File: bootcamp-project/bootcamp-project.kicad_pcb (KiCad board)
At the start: 2 copper layers, 17 parts, among them J3 FTDI, SW1 SW_Push, U1 ATmega328P-A, Y1 16MHz

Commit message: pcb: not viable
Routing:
- net TXO: track 0.00 -> 64.6 mm, vias 0 -> 2
- net MOSI: track 0.00 -> 60.5 mm, vias 0 -> 2
- net D7: track 0.00 -> 54.2 mm
- net D8: track 0.00 -> 53.9 mm, vias 0 -> 1
- net RXI: track 0.00 -> 50.1 mm, vias 0 -> 1
- net RAW: track 0.00 -> 37.7 mm, vias 0 -> 2
- net MISO: track 0.00 -> 31.2 mm, vias 0 -> 1
- net D6: track 0.00 -> 29.9 mm, vias 0 -> 1
- net D5: track 0.00 -> 24.0 mm, vias 0 -> 1
- net D4: track 0.00 -> 16.0 mm, vias 0 -> 1
- net D2: track 0.00 -> 15.4 mm, vias 0 -> 1
- net D3: track 0.00 -> 13.1 mm, vias 0 -> 1
- net GND: track 89.0 -> 92.7 mm, vias 3 -> 2
- net SCK: track 48.2 -> 44.7 mm, vias 1 -> 2
- net DTR: track 57.1 -> 58.5 mm

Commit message: pcb: new try, again
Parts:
- moved R2 24.8 mm to (99.6, 97.5), turned to 135 degrees
- moved C2 22.7 mm to (120.3, 78.7)
- moved D2 20.8 mm to (101.0, 96.1), turned to 135 degrees
- moved C3 18.7 mm to (119.8, 91.2), turned to 0 degrees
- moved R3 15.1 mm to (100.8, 79.1), turned to 0 degrees
- moved R1 10.5 mm to (115.8, 78.8), turned to 0 degrees
- moved D1 9.36 mm to (115.8, 76.4), turned to 0 degrees
- moved SW1 9.28 mm to (119.5, 101.0)
- moved C1 8.31 mm to (119.9, 83.9)
- moved C4 8.06 mm to (112.1, 101.1)
- moved C6 6.10 mm to (106.7, 101.1), turned to 0 degrees
- moved J1 4.00 mm to (95.0, 91.2)
- moved U1 3.61 mm to (109.4, 88.8), turned to -135 degrees
- moved J2 3.00 mm to (125.0, 92.5)
- moved C7 2.01 mm to (102.9, 94.2)
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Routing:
- net MOSI: track 60.5 -> 0.00 mm, vias 2 -> 0
- net D7: track 54.2 -> 0.00 mm
- net D8: track 53.9 -> 0.00 mm, vias 1 -> 0
- net DTR: track 58.5 -> 12.3 mm, vias 2 -> 0
- net SCK: track 44.7 -> 0.00 mm, vias 2 -> 0
- net TXO: track 64.6 -> 23.1 mm, vias 2 -> 0
- net RAW: track 37.7 -> 70.7 mm, vias 2 -> 0
- net MISO: track 31.2 -> 0.00 mm, vias 1 -> 0
- net D6: track 29.9 -> 0.00 mm, vias 1 -> 0
- net D5: track 24.0 -> 0.00 mm, vias 1 -> 0
- net RXI: track 50.1 -> 29.3 mm, vias 1 -> 0
- net D4: track 16.0 -> 0.00 mm, vias 1 -> 0
- net D2: track 15.4 -> 0.00 mm, vias 1 -> 0
- net D3: track 13.1 -> 0.00 mm, vias 1 -> 0
- net Net-(U1-XTAL2/PB7): track 13.0 -> 0.00 mm
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
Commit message: pcb: everything seems connected
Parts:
- moved C2 1.25 mm to (120.3, 80.0)
- moved D1 1.25 mm to (115.8, 77.7)
- moved R1 1.25 mm to (115.8, 80.0)
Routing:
- net DTR: track 12.3 -> 81.1 mm, vias 0 -> 4
- net TXO: track 23.1 -> 76.0 mm, vias 0 -> 1
- net RXI: track 29.3 -> 75.6 mm
- net SCK: track 0.00 -> 39.5 mm, vias 0 -> 3
- net D2: track 0.00 -> 30.7 mm
- net D10: track 0.00 -> 26.5 mm, vias 0 -> 1
- net MOSI: track 0.00 -> 25.6 mm, vias 0 -> 1
- net VCC: track 38.9 -> 62.7 mm, vias 0 -> 2
- net Net-(U1-XTAL2/PB7): track 0.00 -> 22.3 mm, vias 0 -> 2
- net Net-(C1-Pad1): track 0.00 -> 20.6 mm, vias 0 -> 2
- net MISO: track 0.00 -> 20.4 mm, vias 0 -> 1
- net D4: track 0.00 -> 19.0 mm, vias 0 -> 1
- net D3: track 0.00 -> 18.7 mm, vias 0 -> 1
- net A3: track 0.00 -> 18.0 mm, vias 0 -> 1
- net D9: track 0.00 -> 17.8 mm, vias 0 -> 1
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
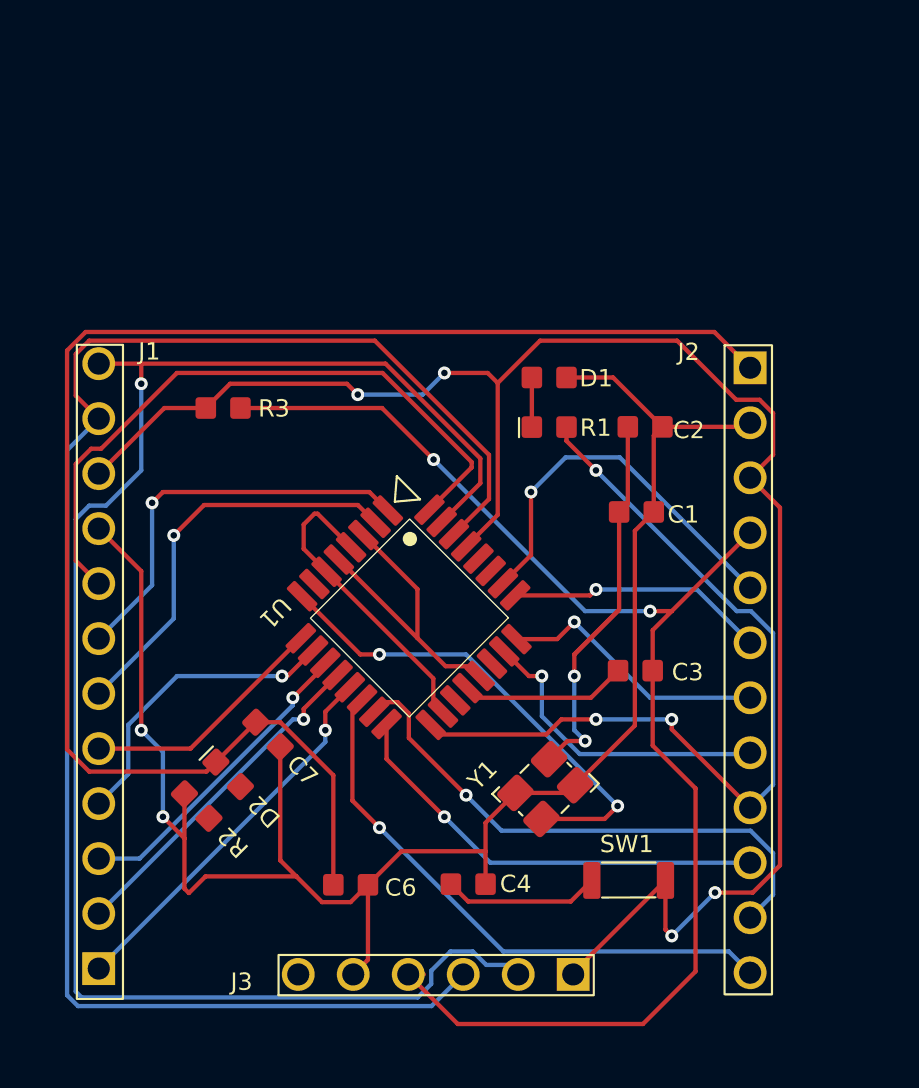
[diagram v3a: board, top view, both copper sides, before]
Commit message: pcb: all connected, no error, no warning
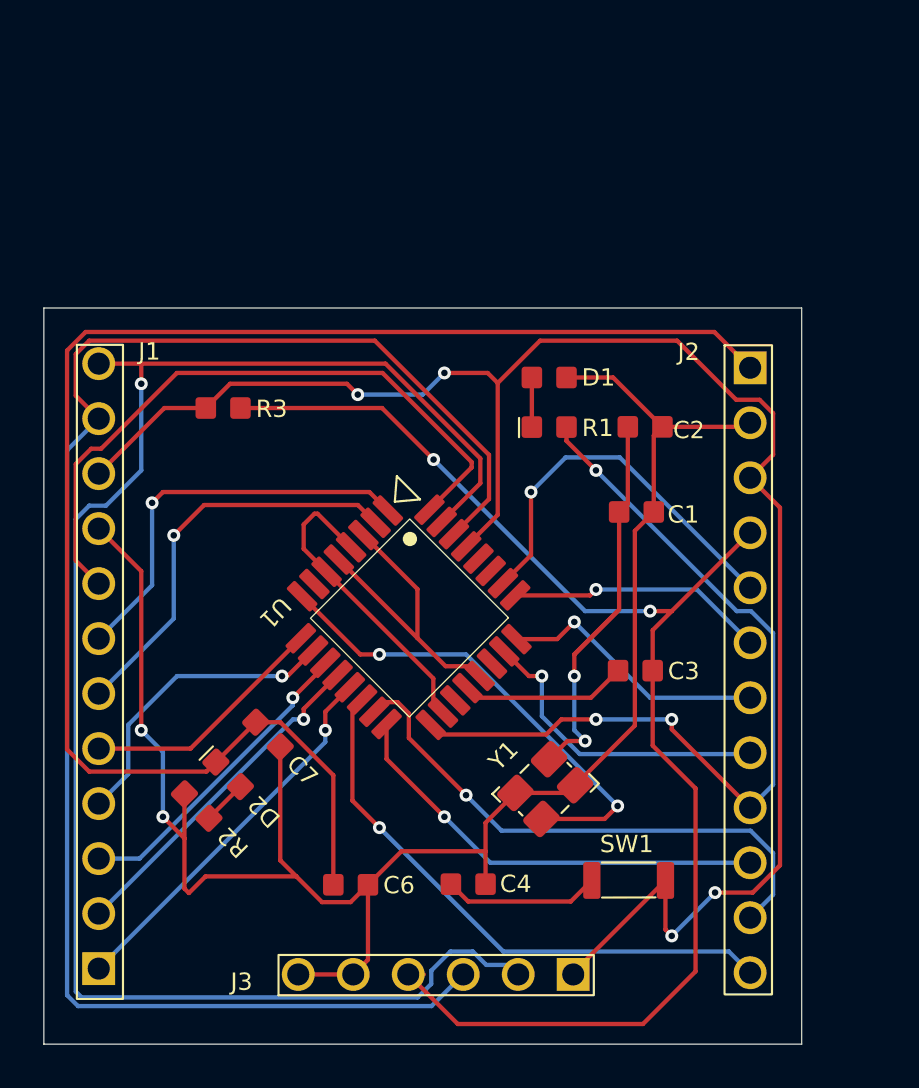
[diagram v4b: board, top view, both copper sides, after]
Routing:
- net GND: track 82.2 -> 84.8 mm
- net Net-(R2-Pad1): track 0.00 -> 2.07 mm
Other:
- board outline added: 35 x 34 mm
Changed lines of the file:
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@@
 		(sheetfile "bootcamp-project.kicad_sch")
 		(attr smd)
-		(fp_poly
-			(pts
-				(xy -1.355 -0.583093) (xy 1.345001 -0.583093) (xy 1.345 0.56) (xy -1.355 0.56)
-			)
+		(fp_rect
+			(start -1.355 -0.583093)
+			(end 1.345 0.56)
 			(stroke
 				(width 0.05)
@@
 		)
 		(fp_text user "R1"
-			(at 1.41 0.49 0)
+			(at 1.5 0.5 0)
 			(unlocked yes)
 			(layer "F.SilkS")
@@
 		)
 		(pad "1" smd roundrect
-			(at -0.81 -0.010001)
+			(at -0.81 -0.01)
 			(size 0.95 1)
 			(layers "F.Cu" "F.Mask" "F.Paste")
@@
 		)
 		(pad "2" smd roundrect
-			(at 0.789999 -0.01)
+			(at 0.79 -0.01)
 			(size 0.95 1)
 			(layers "F.Cu" "F.Mask" "F.Paste")
@@
 		(fp_poly
 			(pts
-				(xy -2 -1.67) (xy -2 1.68) (xy 2.06 1.679999) (xy 2.06 -1.67)
+				(xy -2 -1.67) (xy 2.06 -1.67) (xy 2.06 1.679999) (xy -2 1.68)
 			)
 			(stroke
@@
 		)
 		(fp_text user "Y1"
-			(at -2.265 -2.06 45)
+			(at -0.95 -2.01 45)
 			(unlocked yes)
 			(layer "F.SilkS")
@@
 		(sheetfile "bootcamp-project.kicad_sch")
 		(attr smd)
-		(fp_poly
-			(pts
-				(xy -1.335 -0.579999) (xy 1.355 -0.58) (xy 1.355 0.58) (xy -1.335 0.579999)
-			)
+		(fp_rect
+			(start -1.335 -0.58)
+			(end 1.355 0.58)
 			(stroke
 				(width 0.05)
@@
 		)
 		(fp_text user "C6"
-			(at 1.58 0.61 0)
+			(at 1.5 0.5 0)
 			(unlocked yes)
 			(layer "F.SilkS")
@@
 		)
 		(pad "1" smd roundrect
-			(at -0.799999 0.01)
+			(at -0.8 0.01)
 			(size 0.95 1)
 			(layers "F.Cu" "F.Mask" "F.Paste")
@@
 		)
 		(pad "2" smd roundrect
-			(at 0.799999 0.01)
+			(at 0.8 0.01)
 			(size 0.95 1)
 			(layers "F.Cu" "F.Mask" "F.Paste")
@@
 		(sheetfile "bootcamp-project.kicad_sch")
 		(attr smd)
-		(fp_poly
-			(pts
-				(xy -1.55 -0.56) (xy 1.565 -0.56) (xy 1.565 0.6) (xy -1.55 0.600001)
-			)
+		(fp_rect
+			(start -1.55 -0.56)
+			(end 1.565 0.6)
 			(stroke
 				(width 0.05)
@@
 		)
 		(fp_text user "D1"
-			(at 1.395 0.535 0)
+			(at 1.5 0.5 0)
 			(unlocked yes)
 			(layer "F.SilkS")
@@
 		(sheetfile "bootcamp-project.kicad_sch")
 		(attr smd)
-		(fp_poly
-			(pts
-				(xy -1.335 -0.579999) (xy 1.355 -0.58) (xy 1.355 0.58) (xy -1.335 0.579999)
-			)
+		(fp_rect
+			(start -1.335 -0.58)
+			(end 1.355 0.58)
 			(stroke
 				(width 0.05)
@@
 		)
 		(fp_text user "C3"
-			(at 1.68 0.55 0)
+			(at 1.5 0.5 0)
 			(unlocked yes)
 			(layer "F.SilkS")
@@
 		)
 		(pad "1" smd roundrect
-			(at -0.799999 0.01)
+			(at -0.8 0.01)
 			(size 0.95 1)
 			(layers "F.Cu" "F.Mask" "F.Paste")
@@
 		)
 		(pad "2" smd roundrect
-			(at 0.799999 0.01)
+			(at 0.8 0.01)
 			(size 0.95 1)
 			(layers "F.Cu" "F.Mask" "F.Paste")
@@
 		(sheetfile "bootcamp-project.kicad_sch")
 		(attr smd)
-		(fp_poly
-			(pts
-				(xy -1.355 -0.583093) (xy 1.345001 -0.583093) (xy 1.345 0.56) (xy -1.355 0.56)
-			)
+		(fp_rect
+			(start -1.355 -0.583093)
+			(end 1.345 0.56)
 			(stroke
 				(width 0.05)
@@
 		)
 		(fp_text user "R3"
-			(at 1.61 0.48 0)
+			(at 1.5 0.5 0)
 			(unlocked yes)
 			(layer "F.SilkS")
@@
 		)
 		(pad "1" smd roundrect
-			(at -0.81 -0.010001)
+			(at -0.81 -0.01)
 			(size 0.95 1)
 			(layers "F.Cu" "F.Mask" "F.Paste")
@@
 		)
 		(pad "2" smd roundrect
-			(at 0.789999 -0.01)
+			(at 0.79 -0.01)
 			(size 0.95 1)
 			(layers "F.Cu" "F.Mask" "F.Paste")
@@
 		(layer "F.SilkS")
 	)
+	(gr_rect
+		(start 92.5 74.5)
+		(end 127.5 108.5)
+		(stroke
+			(width 0.05)
+			(type default)
+		)
+		(fill no)
+		(layer "Edge.Cuts")
+	)
 	(segment
 		(start 119.47 79.99)
@@
 	)
 	(segment
+		(start 106.79 105.28)
+		(end 104.25 105.28)
+		(width 0.2)
+		(layer "F.Cu")
+		(net 15)
+	)
+	(segment
 		(start 95.035 84.69)
 		(end 97 86.655)
@@
 	)
 	(segment
+		(start 101.576899 96.604472)
+		(end 100.125685 98.055686)
+		(width 0.2)
+		(layer "F.Cu")
+		(net 27)
+	)
+	(segment
+		(start 100.125685 98.055686)
+		(end 100.125685 98.069828)
+		(width 0.2)
+		(layer "F.Cu")
+		(net 27)
+	)
+	(segment

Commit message: pcb: add ground plane
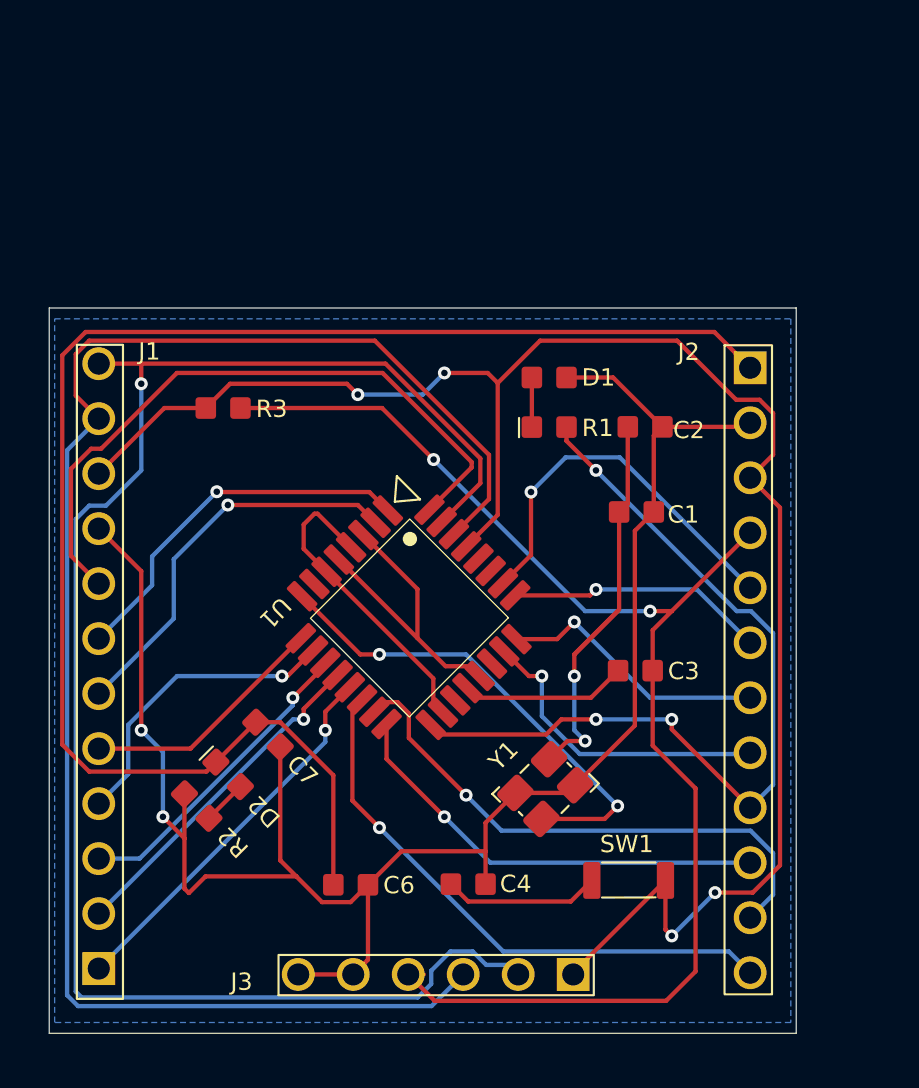
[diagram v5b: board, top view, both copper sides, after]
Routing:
- net D3: track 18.7 -> 17.3 mm
- net VCC: track 62.7 -> 61.8 mm
- net D4: track 19.0 -> 18.3 mm
- added copper zone on B.Cu, net GND
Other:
- board size 35 x 34 mm -> 34.5 x 33.5 mm

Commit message: pcb: remake a clean pcb
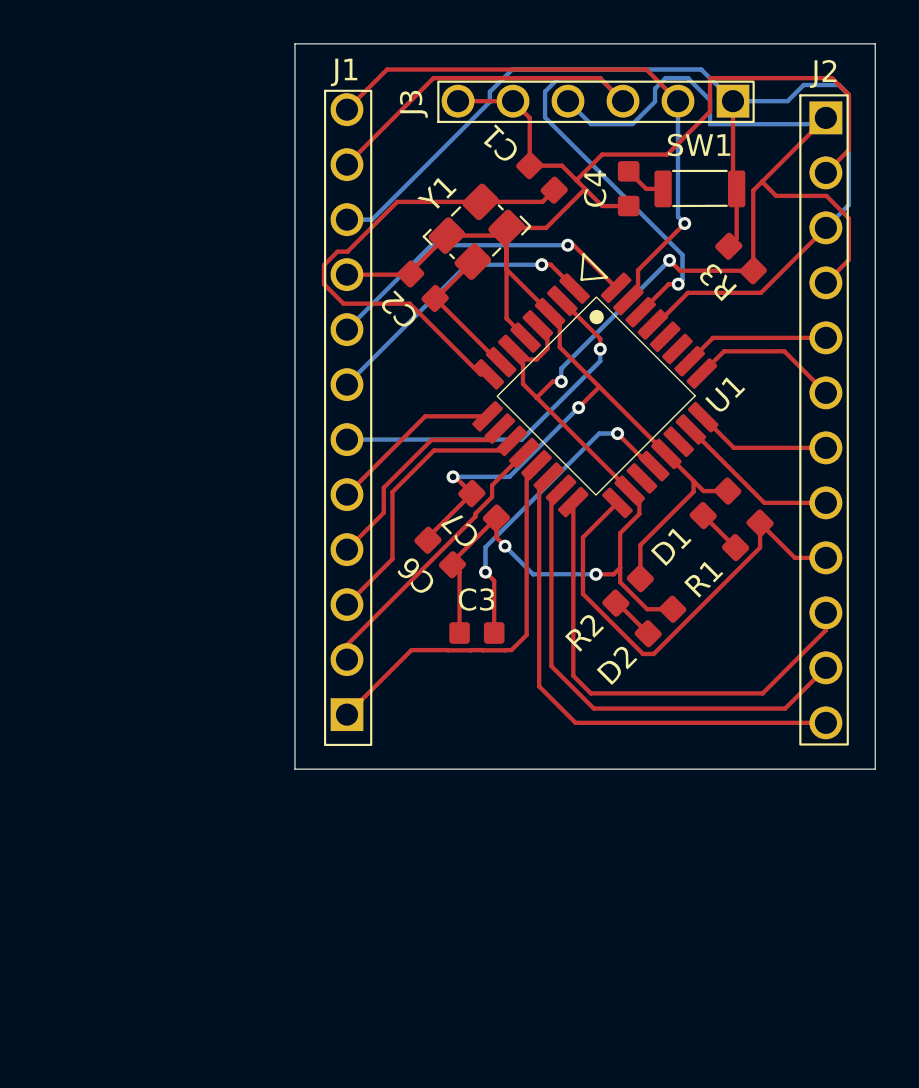
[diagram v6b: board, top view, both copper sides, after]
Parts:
- moved J3 41.0 mm to (118.0, 65.0)
- moved C4 33.0 mm to (119.5, 69.0), turned to 90 degrees
- moved SW1 32.1 mm to (122.8, 69.0)
- moved Y1 25.9 mm to (112.5, 71.0)
- moved R3 24.9 mm to (124.7, 72.2), turned to 135 degrees
- moved R2 22.3 mm to (119.5, 87.6), turned to 45 degrees
- moved D2 21.2 mm to (121.0, 89.0), turned to -135 degrees
- moved J1 16.4 mm to (106.5, 79.5)
- moved C1 16.0 mm to (115.5, 68.5), turned to 135 degrees
- moved C6 15.9 mm to (110.8, 85.8), turned to 135 degrees
- moved C7 14.5 mm to (112.8, 83.6), turned to 135 degrees
- moved J2 13.5 mm to (128.5, 79.5)
- moved U1 13.4 mm to (118.0, 78.5)
- moved C2 12.1 mm to (110.0, 73.5), turned to 135 degrees
- moved R1 10.4 mm to (125.0, 85.0), turned to -135 degrees
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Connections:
- C1 pad 1: Net-(C1-Pad1) -> GND
- C2 pad 1: Net-(C1-Pad1) -> GND
- C6 pad 1: RAW -> GND
- C7 pad 1: RAW -> GND
- D1 pad 1: Net-(D1-Pad0) -> GND
- D2 pad 1: Net-(R2-Pad1) -> Net-(D2-Pad1)
- J2 pad 4: VCC -> RAW
- J3 pad 4: VCC -> RAW
- R2 pad 1: Net-(R2-Pad1) -> GND
- U1 pad 18: Net-(U1-AVCC) -> RAW
- U1 pad 21: Net-(U1-GND) -> GND
- U1 pad 3: Net-(U1-GND) -> GND
- U1 pad 4: Net-(U1-AVCC) -> RAW
- U1 pad 5: Net-(U1-GND) -> GND
- U1 pad 6: Net-(U1-AVCC) -> RAW
- Y1 pad 1: GND -> Net-(U1-XTAL1/PB6)
- Y1 pad 2: Net-(C1-Pad1) -> GND
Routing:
- net VCC: track 61.8 -> 0.00 mm, vias 2 -> 0
- net TXO: track 76.0 -> 27.1 mm
- net RXI: track 75.6 -> 33.0 mm, vias 0 -> 1
- net DTR: track 81.1 -> 50.8 mm, vias 4 -> 0
- net Net-(C1-Pad1): track 20.6 -> 0.00 mm, vias 2 -> 0
- net SCK: track 39.5 -> 21.1 mm, vias 3 -> 0
- net D2: track 30.9 -> 14.9 mm, vias 0 -> 1
- net Net-(U1-GND): track 14.5 -> 0.00 mm
- net Net-(U1-AVCC): track 14.4 -> 0.00 mm
- net A3: track 18.0 -> 6.74 mm, vias 1 -> 0
- net Net-(U1-AREF): track 7.66 -> 14.7 mm, vias 0 -> 2
- net RAW: track 70.9 -> 77.8 mm, vias 0 -> 4
- net Net-(U1-XTAL1/PB6): track 0.00 -> 6.83 mm
- net A0: track 14.4 -> 7.64 mm, vias 1 -> 0
- net A1: track 12.6 -> 6.25 mm, vias 1 -> 0
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- removed copper zone on B.Cu, net GND
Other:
- board size 34.5 x 33.5 mm -> 26.8 x 33.5 mm

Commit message: pcb: pcb done
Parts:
- added G***: LOGO, LOGO, F.Cu at (111.8, 92.8)
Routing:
- added copper zone on B.Cu, net GND

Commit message: add: bonuses
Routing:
- net RAW: track 77.8 -> 78.6 mm
- net GND: track 84.4 -> 85.2 mm
- net Net-(U1-XTAL2/PB7): track 22.3 -> 21.6 mm
- net SCK: track 21.1 -> 20.5 mm
- net D7: track 12.6 -> 12.0 mm
